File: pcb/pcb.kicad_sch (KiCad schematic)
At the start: 8 parts, among them U1 1117-3.3

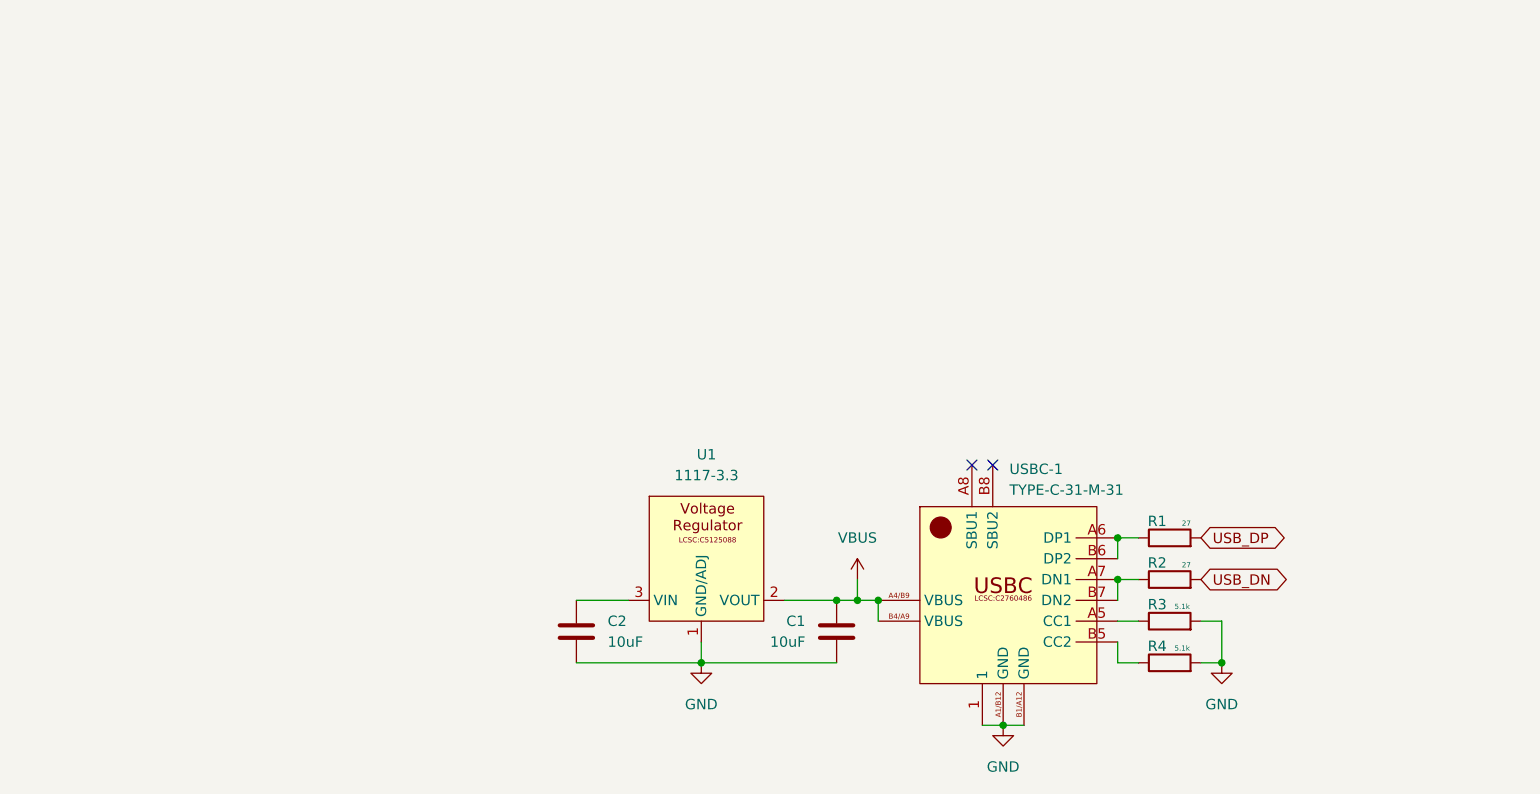
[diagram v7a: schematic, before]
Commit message: work on schematic a bit
- power decoupling
- organize
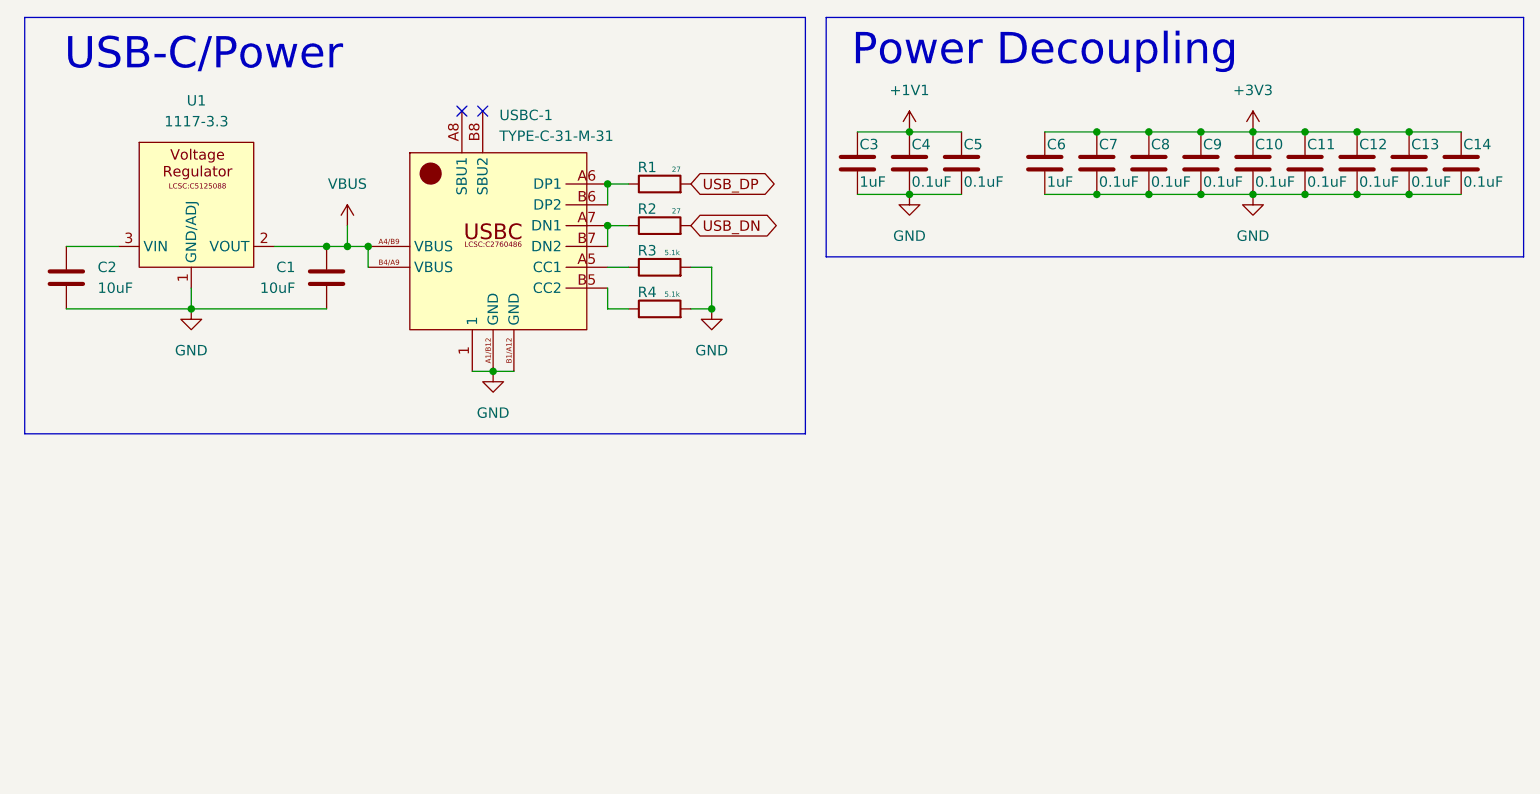
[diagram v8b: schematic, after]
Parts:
- added C10, C11, C12, C13, C14, C4, C5, C7, C8, C9: 0.1uF, Capacitor_SMD:C_0201_0603Metric, symbol Device:C
- added C3, C6: 1uF, Capacitor_SMD:C_0201_0603Metric, symbol Device:C
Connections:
- net GND: now also C10.2, C11.2, C12.2, C13.2, C14.2, C3.2, C4.2, C5.2, C6.2, C7.2, C8.2, C9.2
- new net +1V1: C3.1, C4.1, C5.1
- new net +3V3: C10.1, C11.1, C12.1, C13.1, C14.1, C6.1, C7.1, C8.1, C9.1
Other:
- note added: "Power Decoupling"
- note added: "USB-C/Power"
- moved on the sheet: C1, C2, R1, R2, R3, R4, U1, USBC-1
